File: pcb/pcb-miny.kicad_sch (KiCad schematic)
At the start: 115 parts, among them SW1 Switch, SW10 Switch, SW11 Switch, SW12 Switch, SW13 Switch, SW14 Switch, SW15 Switch, SW16 Switch, SW17 Switch, SW18 Switch, SW19 Switch, SW2 Switch, SW20 Switch, SW21 Switch, SW22 Switch, SW23 Switch, SW24 Switch, SW25 Switch, SW26 Switch, SW27 Switch, SW28 Switch, SW29 Switch, SW3 Switch, SW30 Switch, SW31 Switch, SW32 Switch, SW33 Switch, SW34 Switch, SW4 Switch, SW5 Switch, SW6 Switch, SW7 Switch, SW8 Switch, SW9 Switch

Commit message: miny-v2 draft
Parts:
- removed D7: D, zzkeeb:Diode_1N4148-SOD123, symbol zzkeeb:Diode
- removed FiveWay1: 5Way-Tactile_K1-1506DN-01, zzkeeb:Button_5way, symbol fingerpunch:5Way-Tactile_K1-1506DN-01
- removed H6, H7: MountingHole, zzkeeb:Hole_M2-TH, symbol Mechanical:MountingHole
- removed LED1: YS-SK6812MINI-E, zzkeeb:LED_SK6812-MINI-E, symbol zzkeeb:LED_SK6812MINI-E
- removed MCU1: rp2040-zero, zzkeeb:MCU_rp2040-zero-tht, symbol zzkeeb:MCU_rp2040-zero
- removed SW7: Switch, zzkeeb:Switch_MXKS-miny-hotswap-south-ks3d, symbol zzkeeb:Switch
- added C7: 100n, Capacitor_SMD:C_1206_3216Metric_Pad1.33x1.80mm_HandSolder, symbol Device:C
- added J1: RP2040, zzkeeb:MCU_rp2040-helios, symbol zzkeeb:MCU_rp2040-promicro
- added J2: Conn_01x02_Socket, zzkeeb:Connector_JST-1x02-2.00mm, symbol Connector:Conn_01x02_Socket
- added J3: N!N, zzkeeb:MCU_nice-nano, symbol zzkeeb:MCU_nice-nano
- added JP2: 5V, Jumper:SolderJumper-2_P1.3mm_Open_RoundedPad1.0x1.5mm, symbol Jumper:SolderJumper_2_Open
- added JP4: SolderJumper_2_Open, Jumper:SolderJumper-2_P1.3mm_Open_RoundedPad1.0x1.5mm, symbol Jumper:SolderJumper_2_Open
- added LED31, LED32, LED33, LED34: YS-SK6812MINI-E, zzkeeb:LED_SK6812-MINI-E, symbol zzkeeb:LED_SK6812MINI-E
- added RST1: SW_Push, zzkeeb:Button_SW_SPST_SKQG_WithoutStem, symbol Switch:SW_Push
- added SW34: SW_SPDT, zzkeeb:Switch_SPDT-PCM12, symbol Switch:SW_SPDT
- added VIK_K1: Connector_VIK-keyboard, zzkeeb:Connector_VIK-horizontal-keyboard, symbol vik:vik-keyboard-connector
- renumbered D11 to D10, D12 to D11, D13 to D12, D14 to D13, D15 to D14, D16 to D15, D17 to D16, D18 to D17, D19 to D18, D20 to D19, D21 to D20, D22 to D21, D23 to D22, D24 to D23, D25 to D24, D26 to D25, D27 to D26, D28 to D27, D29 to D28, D30 to D29, D31 to D30, D32 to D31, D33 to D32, D34 to D33, D40 to D34, D8 to D7, D9 to D8, D10 to D9, LED2 to LED1, LED11 to LED10, LED12 to LED11, LED13 to LED12, LED14 to LED13, LED15 to LED14, LED16 to LED15, LED17 to LED16, LED18 to LED17, LED19 to LED18, LED20 to LED19, LED3 to LED2, LED21 to LED20, LED22 to LED21, LED23 to LED22, LED24 to LED23, LED25 to LED24, LED26 to LED25, LED27 to LED26, LED28 to LED27, LED29 to LED28, LED30 to LED29, LED4 to LED3, LED31 to LED30, LED5 to LED4, LED6 to LED5, LED7 to LED6, LED8 to LED7, LED9 to LED8, LED10 to LED9, SW11 to SW10, SW12 to SW11, SW13 to SW12, SW14 to SW13, SW15 to SW14, SW16 to SW15, SW17 to SW16, SW18 to SW17, SW19 to SW18, SW20 to SW19, SW21 to SW20, SW22 to SW21, SW23 to SW22, SW24 to SW23, SW25 to SW24, SW26 to SW25, SW27 to SW26, SW28 to SW27, SW29 to SW28, SW30 to SW29, SW31 to SW30, SW32 to SW31, SW33 to SW32, SW34 to SW33, SW8 to SW7, SW9 to SW8, SW10 to SW9
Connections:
- net +5V: now also C7.1, J1.30 (5V), JP2.1 (A), LED31.1 (VDD), LED32.1 (VDD), LED33.1 (VDD), LED34.1 (VDD), SW34.1 (A); no longer LED1.1 (VDD)
- net GND: now also C7.2, J1.29 (GND), J1.4 (GND), J1.5 (GND), J2.2 (Pin_2), J3.23 (GND), J3.3 (GND), J3.4 (GND), LED31.3 (VSS), LED32.3 (VSS), LED33.3 (VSS), LED34.3 (VSS), RST1.2, VIK_K1.2 (GND)
- net LED: now also LED1.4 (DIN), J1.16 (GP14), JP4.1 (A)
- net col0: now also J1.19 (GP21), J3.2 (008)
- net col1: now also J1.13 (GP9), J3.13 (009)
- net col2: now also J1.12 (GP8), J3.14 (010)
- net col3: now also J1.11 (GP7), J3.15 (111)
- net col4: now also J1.10 (GP6), J3.16 (113)
- net col5: now also J1.9 (GP5), J3.17 (115)
- net col6: now also J1.3 (GP1), J3.18 (002)
- net row0: now also J1.20 (GP23), J3.8 (024)
- net row1: now also J1.21 (GP20), J3.9 (100)
- net row2: now also J1.22 (GP22), J3.10 (011)
- net row3: now also J1.23 (GP26), J3.11 (104)
- net row4: now also J1.24 (GP27), J3.12 (106)
- net at LED30.2 (DOUT): now also LED31.4 (DIN)
- net at D34.1 (K): now also LED1.1 (VDD)
- new net: LED33.2 (DOUT), LED34.4 (DIN)
- new net: LED31.2 (DOUT), LED32.4 (DIN)
- new net: LED32.2 (DOUT), LED33.4 (DIN)
- new net +3.3V: J1.27 (3V3), J3.21 (3V3), VIK_K1.1 (3V3)
- new net BAT: J2.1 (Pin_1), J3.24 (BAT), SW34.2 (B)
- new net GPIO1: J1.26 (GP29), J3.19 (029), VIK_K1.7 (GPIO_AD1)
- new net GPIO2: J1.25 (GP28), J3.20 (031), VIK_K1.9 (GPIO_AD2)
- new net LED_OUT: JP4.2 (B), LED34.2 (DOUT), VIK_K1.5 (RGB_LED_OUT)
- new net RST: J1.28 (RST), J3.22 (RST), RST1.1
- new net SCL: J1.15 (GP13), VIK_K1.4 (SCL)
- new net SDA: J1.14 (GP12), VIK_K1.3 (SDA)
- new net SPI_CLK: J1.6 (GP2), J3.5 (017), VIK_K1.12 (SCLK)
- new net SPI_CS: J1.2 (GP0), J3.1 (006), VIK_K1.10 (SPI_CS)
- new net SPI_MISO: J1.8 (GP4), J3.7 (022), VIK_K1.11 (MISO)
- new net SPI_MOSI: J1.7 (GP3), J3.6 (020), VIK_K1.8 (MOSI)
- new net VIK_5V_1: JP2.2 (B), VIK_K1.6 (5V)
- no-connect marks 8 -> 6
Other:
- moved on the sheet: C4, C5, C6, D1, D10, D11, D12, D13, D14, D15, D16, D17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

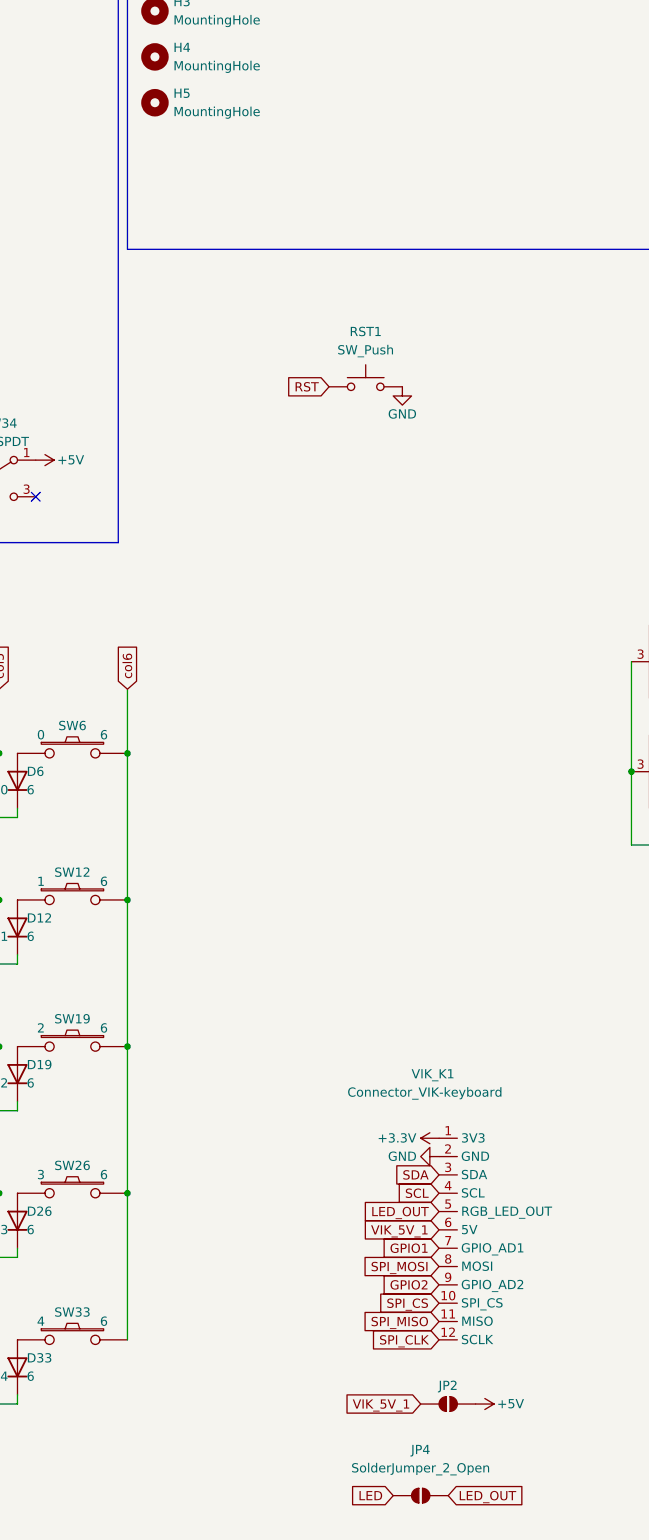
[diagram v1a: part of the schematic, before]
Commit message: add more screw holes, remove rounded pcb
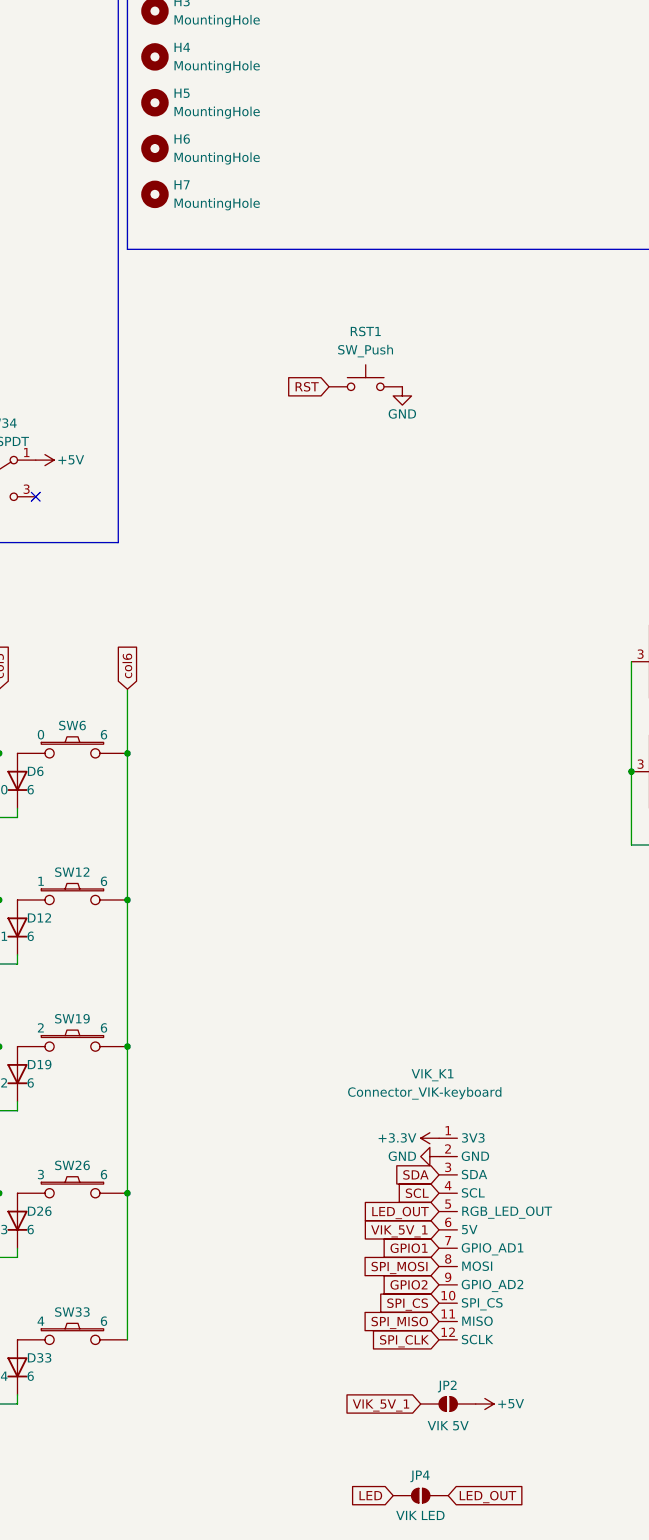
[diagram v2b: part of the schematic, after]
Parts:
- added H6, H7: MountingHole, zzkeeb:Hole_M2, symbol Mechanical:MountingHole
- H1, H2, H3, H4, H5: footprint zzkeeb:Hole_M2-TH -> zzkeeb:Hole_M2
- JP2: value 5V -> VIK 5V
- JP4: value SolderJumper_2_Open -> VIK LED
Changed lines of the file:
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@@
 			)
 		)
-		(property "Footprint" "zzkeeb:Hole_M2-TH"
+		(property "Footprint" "zzkeeb:Hole_M2"
 			(at 161.29 36.83 0)
 			(effects
@@
 			)
 		)
-		(property "Value" "5V"
-			(at 201.93 233.68 0)
+		(property "Value" "VIK 5V"
+			(at 201.93 232.918 0)
 			(effects
 				(font
 					(size 1.27 1.27)
 				)
-				(hide yes)
 			)
 		)
@@
 			)
 		)
-		(property "Footprint" "zzkeeb:Hole_M2-TH"
+		(property "Footprint" "zzkeeb:Hole_M2"
 			(at 161.29 24.13 0)
 			(effects
@@
 	)
 	(symbol
+		(lib_id "Mechanical:MountingHole")
+		(at 161.29 62.23 0)
+		(unit 1)
+		(exclude_from_sim no)
+		(in_bom yes)
+		(on_board yes)
+		(dnp no)
+		(fields_autoplaced yes)
+		(property "Reference" "H7"
+			(at 163.83 60.9599 0)
+			(effects
+				(font
+					(size 1.27 1.27)
+				)
+				(justify left)
+			)
+		)
+		(property "Value" "MountingHole"
+			(at 163.83 63.4999 0)
+			(effects
+				(font
+					(size 1.27 1.27)
+				)
+				(justify left)
+			)
+		)
+		(property "Footprint" "zzkeeb:Hole_M2"
+			(at 161.29 62.23 0)
+			(effects
+				(font
+					(size 1.27 1.27)
+				)
+				(hide yes)
+			)
+		)
+		(property "Datasheet" "~"
+			(at 161.29 62.23 0)
+			(effects
+				(font
+					(size 1.27 1.27)
+				)
+				(hide yes)
+			)
+		)
+		(property "Description" ""
+			(at 161.29 62.23 0)
+			(effects
+				(font
+					(size 1.27 1.27)
+				)
+				(hide yes)
+			)
+		)
+		(instances
+			(project "pcb-miny"
+				(path "/5689f24b-6eca-4ca4-9c6c-dd56b6ced5a9"
+					(reference "H7")
+					(unit 1)
+				)
+			)
+		)
+	)
+	(symbol
 		(lib_id "zzkeeb:Diode")
 		(at 124.46 143.51 0)
@@
 			)
 		)
-		(property "Footprint" "zzkeeb:Hole_M2-TH"
+		(property "Footprint" "zzkeeb:Hole_M2"
 			(at 161.29 30.48 0)
 			(effects
@@
 			)
 		)
-		(property "Footprint" "zzkeeb:Hole_M2-TH"
+		(property "Footprint" "zzkeeb:Hole_M2"
 			(at 161.29 49.53 0)
 			(effects
@@
 		(on_board yes)
 		(dnp no)
-		(fields_autoplaced yes)
 		(property "Reference" "JP4"
-			(at 198.12 236.22 0)
+			(at 198.12 239.776 0)
 			(effects
 				(font
@@
 			)
 		)
-		(property "Value" "SolderJumper_2_Open"
-			(at 198.12 238.76 0)
+		(property "Value" "VIK LED"
+			(at 198.12 245.364 0)
 			(effects
 				(font
@@
 			)
 		)
-		(property "Footprint" "zzkeeb:Hole_M2-TH"
+		(property "Footprint" "zzkeeb:Hole_M2"
 			(at 161.29 43.18 0)
 			(effects
@@
 					(unit 1)
 				)
+			)
+		)
+	)
+	(symbol
+		(lib_id "Mechanical:MountingHole")
+		(at 161.29 55.88 0)
+		(unit 1)
+		(exclude_from_sim no)
+		(in_bom yes)
+		(on_board yes)
+		(dnp no)
+		(fields_autoplaced yes)
+		(property "Reference" "H6"
+			(at 163.83 54.6099 0)
+			(effects
+				(font
+					(size 1.27 1.27)
+				)
+				(justify left)
+			)
+		)
+		(property "Value" "MountingHole"
+			(at 163.83 57.1499 0)
+			(effects
+				(font
+					(size 1.27 1.27)
+				)
+				(justify left)
+			)
+		)
+		(property "Footprint" "zzkeeb:Hole_M2"
+			(at 161.29 55.88 0)
+			(effects
+				(font
+					(size 1.27 1.27)
+				)
+				(hide yes)
+			)
+		)
+		(property "Datasheet" "~"
+			(at 161.29 55.88 0)
+			(effects
+				(font
+					(size 1.27 1.27)
+				)
+				(hide yes)
+			)
+		)
+		(property "Description" ""
+			(at 161.29 55.88 0)
+			(effects
+				(font
+					(size 1.27 1.27)
+				)
+				(hide yes)
+			)
+		)
+		(instances
+			(project "pcb-miny"
+				(path "/5689f24b-6eca-4ca4-9c6c-dd56b6ced5a9"
+					(reference "H6")
+					(unit 1)
+				)
